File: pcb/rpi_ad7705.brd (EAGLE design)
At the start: 39.4 x 51.1 mm, 17 parts

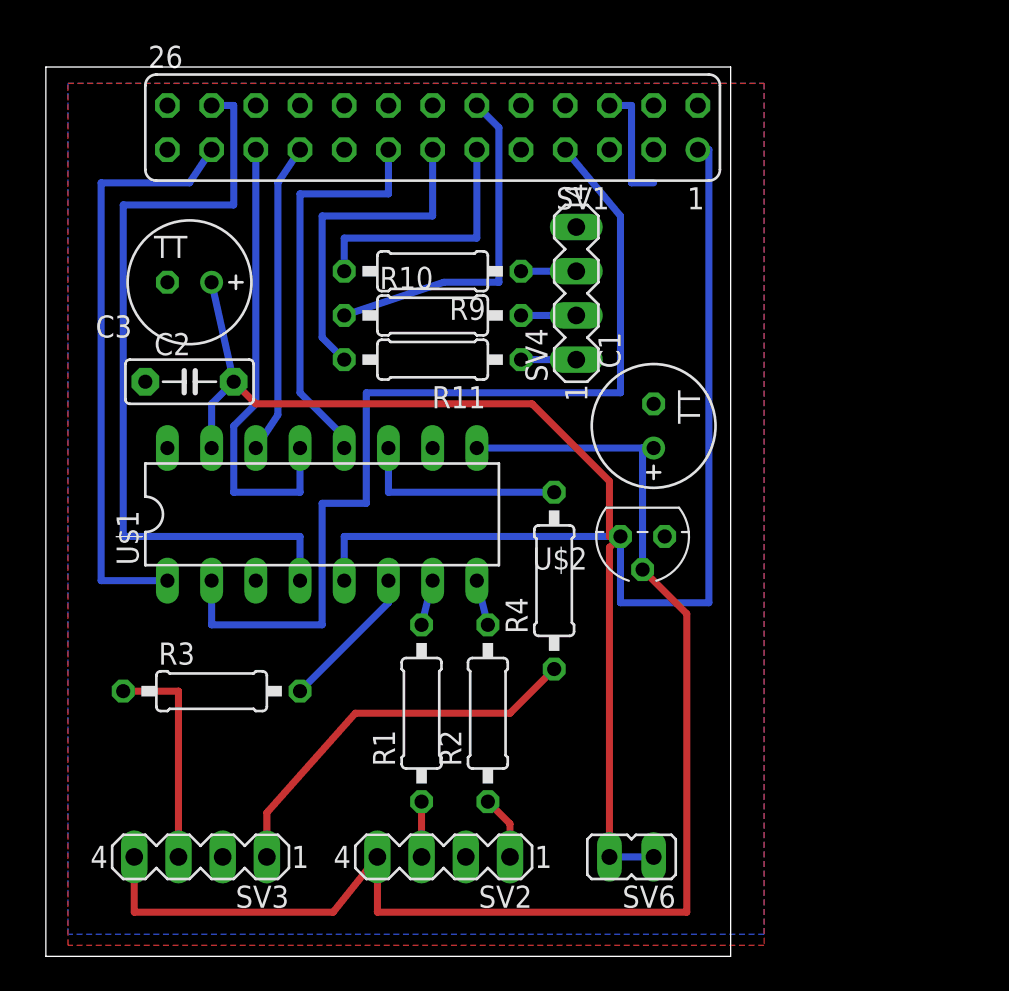
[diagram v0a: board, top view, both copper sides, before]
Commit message: Updated circuit with an oscillator and new pin header.
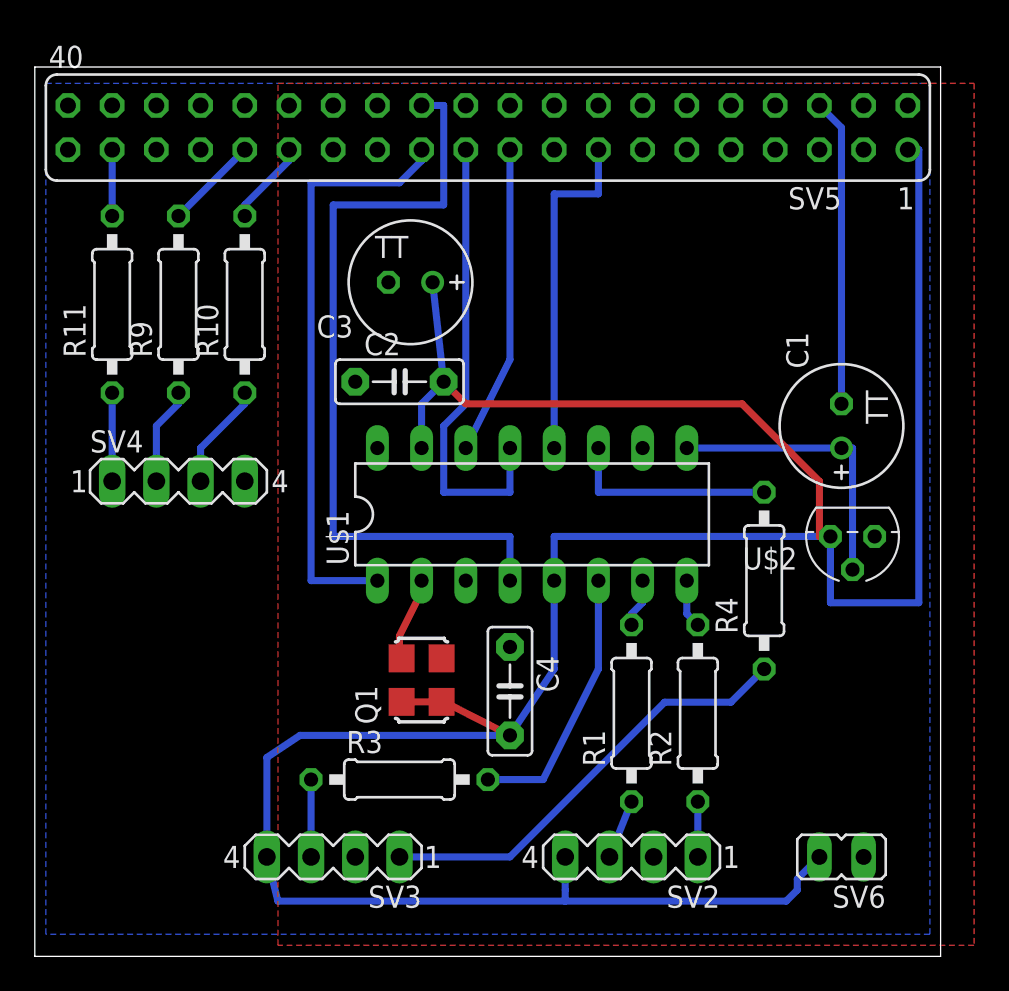
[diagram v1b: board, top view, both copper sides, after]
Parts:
- removed SV1: RASPBERRY PI, con-lsta:FE13-2
- added C4: 0.1uF, capacitor-wima:C5B2.5
- added Q1: 2.4576 MHz, crystal:ASF
- added SV5: (no value), con-lsta:FE20-2
- moved SV4 25.3 mm to (7.62, 27.3), turned to 0 degrees
- moved R11 18.7 mm to (3.81, 37.5), turned to 90 degrees
- moved R9 14.7 mm to (7.62, 37.5), turned to 90 degrees
- moved C3 12.7 mm to (21.0, 38.7)
- moved R2 12.1 mm to (37.5, 14.0)
- moved R1 12.1 mm to (33.7, 14.0)
- moved U$1 12.1 mm to (27.9, 25.4)
- moved C2 12.1 mm to (20.3, 33.0)
- moved R4 12.1 mm to (41.3, 21.6)
- moved SV6 12.1 mm to (45.7, 5.71)
- moved U$2 12.1 mm to (43.8, 24.1)
- moved R3 11.9 mm to (20.3, 10.2)
- moved R10 10.8 mm to (11.4, 37.5), turned to 90 degrees
- moved C1 10.8 mm to (45.7, 30.5)
- moved SV2 10.8 mm to (33.7, 5.71)
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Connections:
- removed net N$18: R9.1, SV4.3
- new net N$22: C1.+, U$1.9, U$2.2
- net +3V3: now also C4.2, Q1.1, Q1.4, SV2.4, SV3.4, SV5.1; no longer SV1.1, SV6.1
- net GND: now also C4.1, Q1.2, SV5.39, SV5.6, SV6.1; no longer SV1.6
- net N$1: now also SV5.19; no longer SV1.19
- net N$15: now also R10.1, SV4.3; no longer R9.2, SV1.11
- net N$16: now also R9.2, SV5.31; no longer R10.1, SV1.12
- net N$17: now also R10.2, SV5.29; no longer R11.2, SV1.13
- net N$2: now also SV5.23; no longer SV1.23
- net N$20: now also R9.1; no longer R10.2
- net N$21: now also SV5.15; no longer SV1.15
- net N$3: now also Q1.3; no longer SV1.7
- net N$4: now also SV5.24; no longer SV1.24
- net N$5: now also R11.2, SV5.37; no longer C1.+, SV2.4, SV3.4, U$1.9, U$2.2
- net N$6: now also SV5.21; no longer SV1.21
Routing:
- net N$5: track 77.5 -> 3.81 mm
- net +3V3: track 113.2 -> 165.9 mm
- net N$3: track 54.5 -> 4.81 mm
- net N$22: track 0.00 -> 16.5 mm
- net N$16: track 19.9 -> 5.39 mm
- net N$17: track 18.9 -> 4.86 mm
- net GND: track 6.98 -> 17.7 mm
- net N$15: track 14.6 -> 6.13 mm
- net N$13: track 12.7 -> 4.45 mm
- net N$9: track 8.45 -> 15.4 mm
- net N$21: track 23.3 -> 19.7 mm
- net N$18: track 3.18 -> 0.00 mm
- net N$14: track 22.7 -> 25.4 mm
- net N$20: track 3.18 -> 5.61 mm
- net N$19: track 3.18 -> 5.08 mm
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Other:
- board size 39.4 x 51.1 mm -> 52 x 51.1 mm

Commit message: Switched the molex to the other side
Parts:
- removed SV6: 3.3V, jumper:JP1
- flipped SV2 to the bottom, turned to 0 degrees
- flipped SV3 to the bottom, turned to 0 degrees
- flipped SV4 to the bottom, turned to 180 degrees
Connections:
- net +3V3: no longer SV6.2
- net GND: no longer SV6.1
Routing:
- net +3V3: track 165.9 -> 135.0 mm
- net N$14: track 25.4 -> 37.4 mm
- net N$15: track 6.13 -> 7.03 mm
- net N$19: track 5.08 -> 5.71 mm
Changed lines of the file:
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@@
 <element name="R10" library="resistor" package="0207/10" value="22R" x="11.43" y="37.465" rot="R90"/>
 <element name="R11" library="resistor" package="0207/10" value="22R" x="3.81" y="37.465" rot="R90"/>
-<element name="SV4" library="con-lstb" package="MA04-1" value="GPIO" x="7.62" y="27.305">
-<attribute name="MF" value="" x="7.62" y="27.305" size="1.778" layer="27" display="off"/>
-<attribute name="MPN" value="" x="7.62" y="27.305" size="1.778" layer="27" display="off"/>
-<attribute name="OC_FARNELL" value="unknown" x="7.62" y="27.305" size="1.778" layer="27" display="off"/>
-<attribute name="OC_NEWARK" value="unknown" x="7.62" y="27.305" size="1.778" layer="27" display="off"/>
+<element name="SV4" library="con-lstb" package="MA04-1" value="GPIO" x="7.62" y="27.305" rot="MR180">
+<attribute name="MF" value="" x="7.62" y="27.305" size="1.778" layer="28" rot="MR180" display="off"/>
+<attribute name="MPN" value="" x="7.62" y="27.305" size="1.778" layer="28" rot="MR180" display="off"/>
+<attribute name="OC_FARNELL" value="unknown" x="7.62" y="27.305" size="1.778" layer="28" rot="MR180" display="off"/>
+<attribute name="OC_NEWARK" value="unknown" x="7.62" y="27.305" size="1.778" layer="28" rot="MR180" display="off"/>
 </element>
 <element name="C3" library="rcl" package="TT2D7" value="1uF/tantalum" x="20.955" y="38.735" rot="R180"/>
-<element name="SV6" library="jumper" package="JP1" value="3.3V" x="45.72" y="5.715" rot="R90"/>
 <element name="C1" library="rcl" package="TT2D7" value="1uF/tantalum" x="45.72" y="30.48" rot="R90"/>
-<element name="SV2" library="con-lstb" package="MA04-1" value="" x="33.655" y="5.715" rot="R180">
-<attribute name="MF" value="" x="33.655" y="5.715" size="1.778" layer="27" rot="R180" display="off"/>
-<attribute name="MPN" value="" x="33.655" y="5.715" size="1.778" layer="27" rot="R180" display="off"/>
-<attribute name="OC_FARNELL" value="unknown" x="33.655" y="5.715" size="1.778" layer="27" rot="R180" display="off"/>
-<attribute name="OC_NEWARK" value="unknown" x="33.655" y="5.715" size="1.778" layer="27" rot="R180" display="off"/>
-</element>
-<element name="SV3" library="con-lstb" package="MA04-1" value="" x="16.51" y="5.715" rot="R180">
-<attribute name="MF" value="" x="16.51" y="5.715" size="1.778" layer="27" rot="R180" display="off"/>
-<attribute name="MPN" value="" x="16.51" y="5.715" size="1.778" layer="27" rot="R180" display="off"/>
-<attribute name="OC_FARNELL" value="unknown" x="16.51" y="5.715" size="1.778" layer="27" rot="R180" display="off"/>
-<attribute name="OC_NEWARK" value="unknown" x="16.51" y="5.715" size="1.778" layer="27" rot="R180" display="off"/>
+<element name="SV2" library="con-lstb" package="MA04-1" value="" x="33.655" y="5.715" rot="MR0">
+<attribute name="MF" value="" x="33.655" y="5.715" size="1.778" layer="28" rot="MR0" display="off"/>
+<attribute name="MPN" value="" x="33.655" y="5.715" size="1.778" layer="28" rot="MR0" display="off"/>
+<attribute name="OC_FARNELL" value="unknown" x="33.655" y="5.715" size="1.778" layer="28" rot="MR0" display="off"/>
+<attribute name="OC_NEWARK" value="unknown" x="33.655" y="5.715" size="1.778" layer="28" rot="MR0" display="off"/>
+</element>
+<element name="SV3" library="con-lstb" package="MA04-1" value="" x="16.51" y="5.715" rot="MR0">
+<attribute name="MF" value="" x="16.51" y="5.715" size="1.778" layer="28" rot="MR0" display="off"/>
+<attribute name="MPN" value="" x="16.51" y="5.715" size="1.778" layer="28" rot="MR0" display="off"/>
+<attribute name="OC_FARNELL" value="unknown" x="16.51" y="5.715" size="1.778" layer="28" rot="MR0" display="off"/>
+<attribute name="OC_NEWARK" value="unknown" x="16.51" y="5.715" size="1.778" layer="28" rot="MR0" display="off"/>
 </element>
 <element name="Q1" library="crystal" package="ASF" value="2.4576 MHz" x="21.59" y="15.875" rot="R90">
@@
 </polygon>
 <polygon width="0.4064" layer="1" isolate="0.8128">
-<vertex x="13.335" y="50.165"/>
-<vertex x="53.34" y="50.165"/>
-<vertex x="53.34" y="0.635"/>
-<vertex x="13.335" y="0.635"/>
+<vertex x="0" y="50.165"/>
+<vertex x="50.8" y="50.165"/>
+<vertex x="50.8" y="0.635"/>
+<vertex x="0" y="0.635"/>
 </polygon>
 <contactref element="Q1" pad="2"/>
 <contactref element="C4" pad="1"/>
 <contactref element="SV5" pad="6"/>
-<contactref element="SV6" pad="1"/>
 <wire x1="44.45" y1="48.895" x2="45.72" y2="47.625" width="0.4064" layer="16"/>
 <wire x1="45.72" y1="47.625" x2="45.72" y2="31.75" width="0.4064" layer="16"/>
@@
 <contactref element="C2" pad="2"/>
 <contactref element="C3" pad="+"/>
-<contactref element="SV6" pad="2"/>
 <wire x1="45.085" y1="20.32" x2="45.085" y2="24.13" width="0.4064" layer="16"/>
 <wire x1="50.165" y1="20.32" x2="50.165" y2="46.355" width="0.4064" layer="16"/>
@@
 <contactref element="SV2" pad="4"/>
 <contactref element="SV3" pad="4"/>
-<wire x1="12.7" y1="5.715" x2="13.335" y2="3.175" width="0.4064" layer="16"/>
-<wire x1="13.335" y1="3.175" x2="29.845" y2="3.175" width="0.4064" layer="16"/>
-<wire x1="26.67" y1="12.7" x2="14.605" y2="12.7" width="0.4064" layer="16"/>
-<wire x1="14.605" y1="12.7" x2="12.7" y2="11.43" width="0.4064" layer="16"/>
-<wire x1="12.7" y1="11.43" x2="12.7" y2="5.715" width="0.4064" layer="16"/>
-<wire x1="29.845" y1="5.715" x2="29.845" y2="3.81" width="0.4064" layer="16"/>
-<wire x1="29.845" y1="3.81" x2="29.845" y2="3.175" width="0.4064" layer="16"/>
-<wire x1="29.845" y1="3.175" x2="42.545" y2="3.175" width="0.4064" layer="16"/>
-<wire x1="42.545" y1="3.175" x2="43.18" y2="3.81" width="0.4064" layer="16"/>
-<wire x1="43.18" y1="3.81" x2="43.18" y2="4.445" width="0.4064" layer="16"/>
-<wire x1="43.18" y1="4.445" x2="44.45" y2="5.715" width="0.4064" layer="16"/>
+<wire x1="20.44" y1="14.625" x2="12.72" y2="14.625" width="0.4064" layer="1"/>
+<wire x1="12.72" y1="14.625" x2="12.7" y2="14.605" width="0.4064" layer="1"/>
+<wire x1="12.7" y1="14.605" x2="12.7" y2="5.715" width="0.4064" layer="1"/>
+<wire x1="26.67" y1="12.7" x2="29.845" y2="12.7" width="0.4064" layer="1"/>
+<wire x1="29.845" y1="12.7" x2="29.845" y2="5.715" width="0.4064" layer="1"/>
 </signal>
 <signal name="N$2">
@@
 <contactref element="R2" pad="1"/>
 <contactref element="SV2" pad="1"/>
-<wire x1="37.465" y1="5.715" x2="37.465" y2="8.89" width="0.4064" layer="16"/>
+<wire x1="37.465" y1="5.715" x2="37.465" y2="8.89" width="0.4064" layer="1"/>
 </signal>
 <signal name="N$13">
 <contactref element="R3" pad="1"/>
 <contactref element="SV3" pad="3"/>
-<wire x1="15.24" y1="10.16" x2="15.24" y2="5.715" width="0.4064" layer="16"/>
+<wire x1="15.24" y1="5.715" x2="15.24" y2="10.16" width="0.4064" layer="1"/>
 </signal>
 <signal name="N$14">
 <contactref element="R4" pad="1"/>
 <contactref element="SV3" pad="1"/>
-<wire x1="20.32" y1="5.715" x2="26.67" y2="5.715" width="0.4064" layer="16"/>
-<wire x1="26.67" y1="5.715" x2="35.56" y2="14.605" width="0.4064" layer="16"/>
-<wire x1="35.56" y1="14.605" x2="39.37" y2="14.605" width="0.4064" layer="16"/>
-<wire x1="39.37" y1="14.605" x2="41.275" y2="16.51" width="0.4064" layer="16"/>
+<wire x1="20.32" y1="5.715" x2="20.32" y2="2.54" width="0.4064" layer="1"/>
+<wire x1="20.32" y1="2.54" x2="40.005" y2="2.54" width="0.4064" layer="1"/>
+<wire x1="40.005" y1="2.54" x2="41.275" y2="3.81" width="0.4064" layer="1"/>
+<wire x1="41.275" y1="3.81" x2="41.275" y2="16.51" width="0.4064" layer="1"/>
 </signal>
 <signal name="N$11">
 <contactref element="R1" pad="1"/>
 <contactref element="SV2" pad="3"/>
-<wire x1="32.385" y1="5.715" x2="33.655" y2="8.89" width="0.4064" layer="16"/>
+<wire x1="32.385" y1="5.715" x2="32.385" y2="7.62" width="0.4064" layer="1"/>
+<wire x1="32.385" y1="7.62" x2="33.655" y2="8.89" width="0.4064" layer="1"/>
 </signal>
 <signal name="N$19">
 <contactref element="SV4" pad="1"/>
 <contactref element="R11" pad="1"/>
-<wire x1="3.81" y1="32.385" x2="3.81" y2="27.305" width="0.4064" layer="16"/>
+<wire x1="3.81" y1="32.385" x2="3.81" y2="27.305" width="0.4064" layer="1"/>
+<wire x1="3.81" y1="26.67" x2="3.81" y2="27.305" width="0.4064" layer="1"/>
 </signal>
 <signal name="N$20">
 <contactref element="SV4" pad="2"/>
 <contactref element="R9" pad="1"/>
-<wire x1="7.62" y1="32.385" x2="7.62" y2="31.75" width="0.4064" layer="16"/>
-<wire x1="7.62" y1="31.75" x2="6.35" y2="30.48" width="0.4064" layer="16"/>
-<wire x1="6.35" y1="30.48" x2="6.35" y2="27.305" width="0.4064" layer="16"/>
+<wire x1="7.62" y1="32.385" x2="7.62" y2="31.115" width="0.4064" layer="1"/>
+<wire x1="7.62" y1="31.115" x2="6.35" y2="29.845" width="0.4064" layer="1"/>
+<wire x1="6.35" y1="29.845" x2="6.35" y2="27.305" width="0.4064" layer="1"/>
 </signal>
 <signal name="N$21">
@@
 <contactref element="SV4" pad="3"/>
 <contactref element="R10" pad="1"/>
-<wire x1="11.43" y1="32.385" x2="11.43" y2="31.75" width="0.4064" layer="16"/>
-<wire x1="11.43" y1="31.75" x2="8.89" y2="29.21" width="0.4064" layer="16"/>
-<wire x1="8.89" y1="29.21" x2="8.89" y2="27.305" width="0.4064" layer="16"/>
+<wire x1="11.43" y1="32.385" x2="8.89" y2="29.845" width="0.4064" layer="1"/>
+<wire x1="8.89" y1="29.845" x2="8.89" y2="27.94" width="0.4064" layer="1"/>
+<wire x1="8.89" y1="27.94" x2="9.525" y2="27.305" width="0.4064" layer="1"/>
+<wire x1="9.525" y1="27.305" x2="8.89" y2="27.305" width="0.4064" layer="1"/>
 </signal>
 <signal name="N$16">
@@
 </signal>
 </signals>
-<errors>
-</errors>
 </board>
 </drawing>
